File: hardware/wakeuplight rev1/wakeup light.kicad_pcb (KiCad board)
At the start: 2 copper layers, 50 x 50 mm, 20 parts, among them CON1 BARREL_JACK, CON2 Fog_Light, CON3 LED_Header, J1 Serial_Header, J2 1/8_MH, J3 1/8_MH, J4 1/8_MH, J5 1/8_MH, SW1 Rotary_Encoder, U1 Arduino_Pro_Mini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

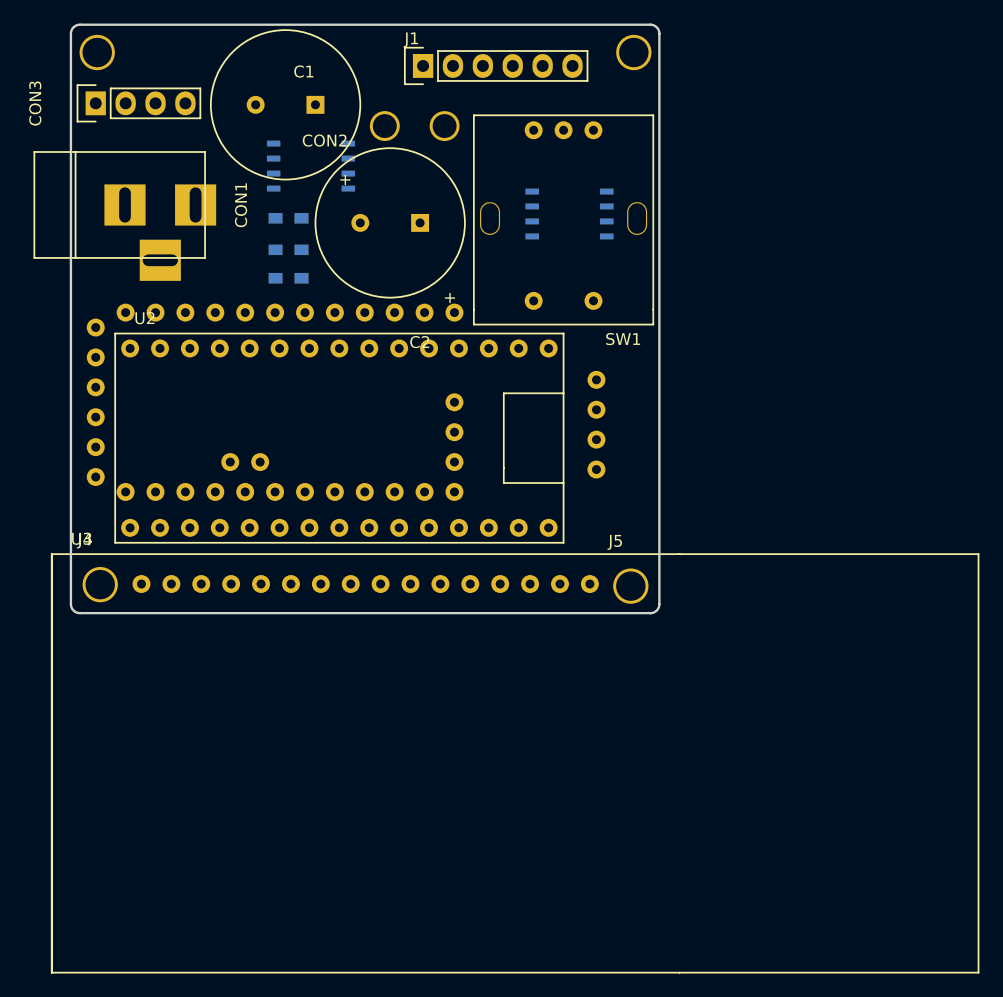
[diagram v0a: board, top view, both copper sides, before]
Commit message: Completed layout
Wiring complete
Need to double check and send off to manufacture.
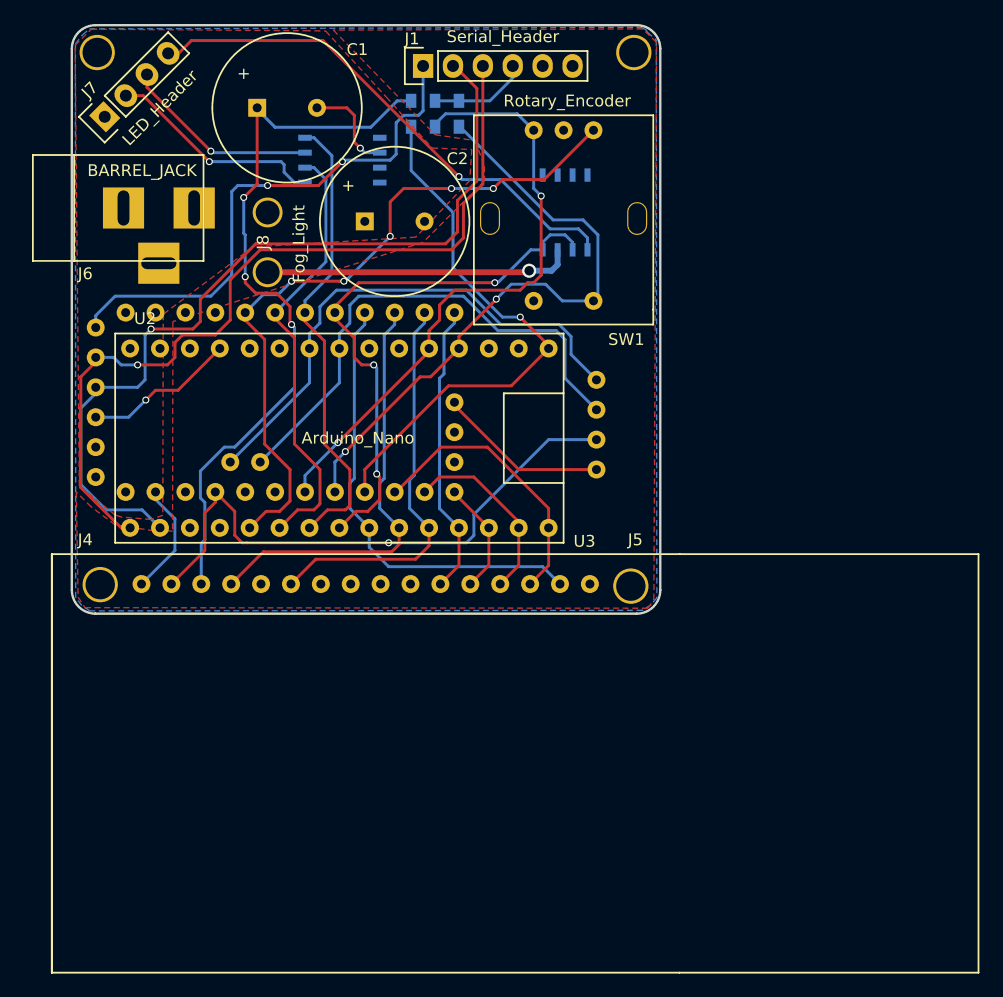
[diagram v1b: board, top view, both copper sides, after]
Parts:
- removed CON1: BARREL_JACK, Connect:BARREL_JACK
- removed CON2: Fog_Light, wakeuplight rev1:Fog_Light
- removed CON3: LED_Header, Pin_Headers:Pin_Header_Straight_1x04
- added J6: BARREL_JACK, Connect:BARREL_JACK, F.Cu at (61.1, 68.6)
- added J7: LED_Header, Pin_Headers:Pin_Header_Straight_1x04, F.Cu at (59.7, 60.8)
- added J8: Fog_Light, wakeuplight rev1:Fog_Light, F.Cu at (73.5, 69.0)
- moved R3 17.4 mm to (85.7, 60.6), turned to 270 degrees
- moved R2 17.0 mm to (89.8, 60.6), turned to 270 degrees
- moved R1 17.0 mm to (87.8, 60.6), turned to 270 degrees
- moved C1 5.69 mm to (72.6, 61.3), turned to 0 degrees
- moved C2 5.28 mm to (81.8, 71.0), turned to 0 degrees
- moved U5 2.71 mm to (79.9, 64.5)
- moved U4 0.40 mm to (98.8, 69.0), turned to 180 degrees
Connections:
- U1 pad 19: Net-(U1-Pad19) -> /RX
- U1 pad 20: Net-(U1-Pad20) -> /TX
- U1 pad 22: /TX -> Net-(U1-Pad22)
- U1 pad 23: /RX -> Net-(U1-Pad23)
- U4 pad 3: Net-(CON2-Pad2) -> /FogLightReturn
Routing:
- net /RX: track 0.00 -> 73.0 mm, vias 0 -> 1
- net /TX: track 0.00 -> 71.3 mm, vias 0 -> 1
- net +5V: track 0.00 -> 70.9 mm, vias 0 -> 2
- net Net-(C1-Pad1): track 0.00 -> 62.7 mm, vias 0 -> 3
- net /D2: track 0.00 -> 59.8 mm, vias 0 -> 5
- net /A0: track 0.00 -> 53.3 mm, vias 0 -> 2
- net /A1: track 0.00 -> 52.4 mm, vias 0 -> 2
- net /D5: track 0.00 -> 47.6 mm, vias 0 -> 3
- net /D13: track 0.00 -> 46.4 mm, vias 0 -> 1
- net Net-(J1-Pad1): track 0.00 -> 45.7 mm, vias 0 -> 2
- net /SCL: track 0.00 -> 44.5 mm
- net Net-(J7-Pad4): track 0.00 -> 44.0 mm, vias 0 -> 1
- net /SDA: track 0.00 -> 43.7 mm
- net /D4: track 0.00 -> 39.4 mm
- net /D6: track 0.00 -> 39.2 mm
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- added copper zone on F.Cu, net +12V
- added copper zone on F.Cu, net +5V
- added copper zone on B.Cu, net GND
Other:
- outline, holes or cut-outs redrawn
- net class 5Acurrent added: clearance 0.2, trace_width 0.5, via_dia 1.2, via_drill 0.8

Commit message: Boards ordered!
gerbers generated and are on the way.
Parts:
- moved C2 0.74 mm to (81.4, 70.4)
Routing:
- net GND: track 32.5 -> 36.7 mm, vias 1 -> 2
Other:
- outline, holes or cut-outs redrawn
- board text added: "Wake-up Light Rev 1.0 Designed in ON, Canada"
- board text added: "YQ"
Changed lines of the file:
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@@
   (general
     (links 86)
-    (no_connects 2)
-    (area 56.796799 52.950799 106.996801 103.150801)
+    (no_connects 0)
+    (area 37.742819 44.958247 138.578001 134.0032)
     (thickness 1.6)
-    (drawings 9)
-    (tracks 378)
+    (drawings 19)
+    (tracks 383)
     (zones 0)
     (modules 20)
@@
   (layers
     (0 F.Cu signal)
-    (31 B.Cu signal hide)
+    (31 B.Cu signal)
     (32 B.Adhes user hide)
     (33 F.Adhes user hide)
@@
     (42 Eco1.User user hide)
     (43 Eco2.User user hide)
-    (44 Edge.Cuts user)
+    (44 Edge.Cuts user hide)
     (45 Margin user hide)
     (46 B.CrtYd user hide)
@@
     (pad_to_mask_clearance 0.2)
     (aux_axis_origin 0 0)
-    (visible_elements FFFFFF7F)
+    (visible_elements 7FFFFF7F)
     (pcbplotparams
-      (layerselection 0x00030_80000001)
-      (usegerberextensions false)
+      (layerselection 0x010fc_80000001)
+      (usegerberextensions true)
       (excludeedgelayer true)
       (linewidth 0.100000)
       (plotframeref false)
-      (viasonmask false)
+      (viasonmask true)
       (mode 1)
       (useauxorigin false)
@@
       (outputformat 1)
       (mirror false)
-      (drillshape 1)
+      (drillshape 0)
       (scaleselection 1)
-      (outputdirectory ""))
+      (outputdirectory gerbers/))
   )
   (net 0 "")
@@
     (add_net /FogLightReturn)
   )
+  (module "wakeuplight rev1:Cap_Fat_1000uF_25V" (layer F.Cu)
+    (at 81.407 70.358)
+    (fp_text reference C2 (at 7.874 -6.604) (layer F.SilkS)
+      (effects (font (size 1 1) (thickness 0.15)))
+    )
+    (fp_text value CP (at 3.81 12.319) (layer F.Fab) hide
+      (effects (font (size 1 1) (thickness 0.15)))
+    )
+    (fp_text user + (at -1.397 -4.318) (layer F.SilkS)
+      (effects (font (size 1 1) (thickness 0.15)))
+    )
+    (fp_circle (center 2.54 -1.27) (end -3.81 -1.27) (layer F.SilkS) (width 0.15))
+    (pad 1 thru_hole rect (at 0 -1.27) (size 1.524 1.524) (drill 0.762) (layers *.Cu *.Mask F.SilkS)
+      (net 3 +12V))
+    (pad 2 thru_hole circle (at 5.08 -1.27) (size 1.524 1.524) (drill 0.762) (layers *.Cu *.Mask F.SilkS)
+      (net 2 GND))
+  )
   (module Pin_Headers:Pin_Header_Straight_1x04 (layer F.Cu)
     (at 59.69 60.833 135)
@@
   (module "wakeuplight rev1:Arduino_Nano" (layer F.Cu)
     (at 80.899 86.868)
-    (fp_text reference U2 (at -17.78 -8.89) (layer F.SilkS)
+    (fp_text reference U2 (at -21.844 7.493) (layer F.SilkS)
       (effects (font (size 1 1) (thickness 0.15)))
     )
@@
       (net 2 GND))
   )
-  (module "wakeuplight rev1:Cap_Fat_1000uF_25V" (layer F.Cu)
-    (at 81.788 70.993)
-    (fp_text reference C2 (at 7.874 -6.604) (layer F.SilkS)
-      (effects (font (size 1 1) (thickness 0.15)))
-    )
-    (fp_text value CP (at 3.81 12.319) (layer F.Fab) hide
-      (effects (font (size 1 1) (thickness 0.15)))
-    )
-    (fp_text user + (at -1.397 -4.318) (layer F.SilkS)
-      (effects (font (size 1 1) (thickness 0.15)))
-    )
-    (fp_circle (center 2.54 -1.27) (end -3.81 -1.27) (layer F.SilkS) (width 0.15))
-    (pad 1 thru_hole rect (at 0 -1.27) (size 1.524 1.524) (drill 0.762) (layers *.Cu *.Mask F.SilkS)
-      (net 3 +12V))
-    (pad 2 thru_hole circle (at 5.08 -1.27) (size 1.524 1.524) (drill 0.762) (layers *.Cu *.Mask F.SilkS)
-      (net 2 GND))
-  )
   (module Pin_Headers:Pin_Header_Straight_1x06 (layer F.Cu)
     (at 86.741 56.515 90)
@@
       (effects (font (size 1 1) (thickness 0.15)))
     )
-    (fp_text value Serial_Header (at 2.4892 6.7818 180) (layer F.SilkS)
+    (fp_text value Serial_Header (at 2.286 7.366 180) (layer F.SilkS)
       (effects (font (size 1 1) (thickness 0.15)))
     )
@@
     (tags "resistor 0603")
     (attr smd)
-    (fp_text reference R1 (at 0 1.9 270) (layer B.SilkS)
+    (fp_text reference R1 (at 3.175 0 270) (layer B.SilkS)
       (effects (font (size 1 1) (thickness 0.15)) (justify mirror))
     )
@@
     (tags "resistor 0603")
     (attr smd)
-    (fp_text reference R2 (at 0 1.9 270) (layer B.SilkS)
+    (fp_text reference R2 (at 3.175 0 270) (layer B.SilkS)
       (effects (font (size 1 1) (thickness 0.15)) (justify mirror))
     )
@@
     (tags "resistor 0603")
     (attr smd)
-    (fp_text reference R3 (at 0 1.9 270) (layer B.SilkS)
+    (fp_text reference R3 (at 3.175 0 270) (layer B.SilkS)
       (effects (font (size 1 1) (thickness 0.15)) (justify mirror))
     )
@@
   (module "wakeuplight rev1:LCD_16x2" (layer F.Cu)
     (at 62.8142 133.5532)
-    (fp_text reference U3 (at 37.6428 -36.6522) (layer F.SilkS)
+    (fp_text reference U3 (at -4.0132 -36.3982) (layer F.SilkS)
       (effects (font (size 1 1) (thickness 0.15)))
     )
@@
     (tags "CMS SOJ")
     (attr smd)
-    (fp_text reference U4 (at 3.3274 0.2032 270) (layer B.SilkS)
+    (fp_text reference U4 (at 3.937 0.127 270) (layer B.SilkS)
       (effects (font (size 1 1) (thickness 0.15)) (justify mirror))
     )
@@
     (tags "CMS SOJ")
     (attr smd)
-    (fp_text reference U5 (at 3.3528 0.254 180) (layer B.SilkS)
+    (fp_text reference U5 (at 3.683 0.254 180) (layer B.SilkS)
       (effects (font (size 1 1) (thickness 0.15)) (justify mirror))
     )
@@
   (module "wakeuplight rev1:2.5mm_MH" (layer F.Cu)
     (at 59.309 100.584)
-    (fp_text reference J4 (at -1.27 -3.81) (layer F.SilkS)
+    (fp_text reference J4 (at -5.969 -2.159) (layer F.SilkS) hide
       (effects (font (size 1 1) (thickness 0.15)))
     )
@@
   (module "wakeuplight rev1:2.5mm_MH" (layer F.Cu)
     (at 104.394 100.711)
-    (fp_text reference J5 (at 0.381 -3.937) (layer F.SilkS)
+    (fp_text reference J5 (at 6.731 -5.588) (layer F.SilkS) hide
       (effects (font (size 1 1) (thickness 0.15)))
     )
@@
   (module "wakeuplight rev1:Fog_Light" (layer F.Cu)
     (at 73.533 68.961 270)
-    (fp_text reference J8 (at 2.54 0.381 270) (layer F.SilkS)
+    (fp_text reference J8 (at 2.54 2.032 270) (layer F.SilkS)
       (effects (font (size 1 1) (thickness 0.15)))
     )
@@
       (net 48 /FogLightReturn))
   )
+  (gr_arc (start 104.8968 55.0508) (end 104.8968 53.0508) (angle 90) (layer F.SilkS) (width 0.2))
   (gr_line (start 106.8968 55.0508) (end 106.8968 101.0508) (angle 90) (layer Edge.Cuts) (width 0.2))
+  (gr_arc (start 104.8968 101.0508) (end 106.8968 101.0508) (angle 90) (layer F.SilkS) (width 0.2))
+  (gr_line (start 104.8968 103.0508) (end 58.8968 103.0508) (angle 90) (layer F.SilkS) (width 0.2))
+  (gr_line (start 56.8968 101.0508) (end 56.8968 55.0508) (angle 90) (layer F.SilkS) (width 0.2))
+  (gr_arc (start 58.8968 55.0508) (end 56.8968 55.0508) (angle 90) (layer Edge.Cuts) (width 0.2))
+  (gr_line (start 58.8968 53.0508) (end 104.8968 53.0508) (angle 90) (layer F.SilkS) (width 0.2))
+  (gr_text YQ (at 103.632 96.266) (layer B.SilkS)
+    (effects (font (size 1.5 1.5) (thickness 0.3)))
+  )
+  (gr_text YQ (at 103.632 96.266) (layer F.SilkS)
+    (effects (font (size 1.5 1.5) (thickness 0.3)) (justify mirror))
+  )
+  (gr_text "Wake-up Light\nRev 1.0\nDesigned in ON, Canada" (at 76.327 56.007) (layer B.SilkS)
+    (effects (font (size 0.6 0.6) (thickness 0.15)) (justify mirror))
+  )
+  (gr_line (start 106.8968 55.0508) (end 106.8968 101.0508) (angle 90) (layer F.SilkS) (width 0.2))
   (gr_line (start 58.8968 53.0508) (end 104.8968 53.0508) (angle 90) (layer Edge.Cuts) (width 0.2))
   (gr_line (start 56.8968 101.0508) (end 56.8968 55.0508) (angle 90) (layer Edge.Cuts) (width 0.2))
-  (gr_line (start 104.8968 103.0508) (end 58.8968 103.0508) (angle 90) (layer Edge.Cuts) (width 0.2))
+  (gr_line (start 104.8968 103.0508) (end 58.8968 103.0508) (angle 90) (layer F.SilkS) (width 0.2))
   (gr_arc (start 104.8968 55.0508) (end 104.8968 53.0508) (angle 90) (layer Edge.Cuts) (width 0.2))
-  (gr_arc (start 58.8968 55.0508) (end 56.8968 55.0508) (angle 90) (layer Edge.Cuts) (width 0.2))
-  (gr_arc (start 58.8968 101.0508) (end 58.8968 103.0508) (angle 90) (layer Edge.Cuts) (width 0.2))
+  (gr_arc (start 58.8968 55.0508) (end 56.8968 55.0508) (angle 90) (layer F.SilkS) (width 0.2))
+  (gr_arc (start 58.8968 101.0508) (end 58.8968 103.0508) (angle 90) (layer F.SilkS) (width 0.2))
   (gr_arc (start 104.8968 101.0508) (end 106.8968 101.0508) (angle 90) (layer Edge.Cuts) (width 0.2))
   (gr_line (start 106.06532 103.00716) (end 106.06532 103.01224) (angle 90) (layer F.Fab) (width 0.2))
@@
   (segment (start 82.296 61.722) (end 84.539 59.479) (width 0.25) (layer B.Cu) (net 1))
   (segment (start 84.539 59.479) (end 85.725 59.479) (width 0.25) (layer B.Cu) (net 1))
+  (segment (start 83.058 65.151) (end 83.058 66.421) (width 0.25) (layer B.Cu) (net 2))
+  (segment (start 83.058 65.151) (end 82.042 65.151) (width 0.25) (layer B.Cu) (net 2))
+  (segment (start 81.407 64.516) (end 81.407 63.5) (width 0.25) (layer F.Cu) (net 2))
+  (segment (start 82.042 65.151) (end 81.407 64.516) (width 0.25) (layer F.Cu) (net 2))
+  (via (at 82.042 65.151) (size 0.6) (drill 0.4) (layers F.Cu B.Cu) (net 2))
+  (segment (start 89.408 85.09) (end 89.408 85.344) (width 0.25) (layer F.Cu) (net 2))
+  (segment (start 89.408 85.344) (end 94.869 90.805) (width 0.25) (layer F.Cu) (net 2))
+  (segment (start 94.869 90.805) (end 101.473 90.805) (width 0.25) (layer F.Cu) (net 2))
   (segment (start 64.008 92.71) (end 64.008 93.345) (width 0.25) (layer B.Cu) (net 2))
   (segment (start 64.008 93.345) (end 65.659 94.996) (width 0.25) (layer B.Cu) (net 2))
   (segment (start 65.659 94.996) (end 65.659 97.6884) (width 0.25) (layer B.Cu) (net 2))
   (segment (start 65.659 97.6884) (end 62.8142 100.5332) (width 0.25) (layer B.Cu) (net 2))
-  (segment (start 89.408 85.09) (end 89.408 85.344) (width 0.25) (layer F.Cu) (net 2))
-  (segment (start 89.408 85.344) (end 94.869 90.805) (width 0.25) (layer F.Cu) (net 2))
-  (segment (start 94.869 90.805) (end 101.473 90.805) (width 0.25) (layer F.Cu) (net 2))
   (segment (start 77.724 60.071) (end 80.264 60.071) (width 0.25) (layer F.Cu) (net 2))
   (segment (start 81.788 63.881) (end 83.058 63.881) (width 0.25) (layer B.Cu) (net 2))
